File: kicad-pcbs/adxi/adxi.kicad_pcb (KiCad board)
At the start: 4 copper layers, 129.7 x 130 mm, 463 parts, among them J1 BNC, J2 PA-SUPPLY, J3 USBC, J4 PA-DRAIN, J5 USB2 Type-A, J6 RFC-GND, J7 12-24V SUPPLY, Q1 MMBF170, Q2 HY1904C2, Q3 2N7002, Q33 2N7002, Q34 HY1904C2, Q35 2N7002, Q36 HY1904C2, Q37 2N7002, Q38 HY1904C2, Q39 2N7002, Q4 HY1904C2, Q40 HY1904C2, Q41 2N7002, Q42 HY1904C2, Q43 2N7002, Q44 HY1904C2, Q45 2N7002, Q46 HY1904C2, Q47 2N7002, Q48 HY1904C2, Q49 2N7002, Q50 HY1904C2, Q51 2N7002, Q52 HY1904C2, Q53 2N7002, Q54 HY1904C2, Q55 2N7002, Q56 HY1904C2, Q57 2N7002, Q58 HY1904C2, Q59 2N7002, Q60 HY1904C2, U1 SI5351A-B-GTR, U10 CM108B, U11 93C46, U2 CD2003, U4 74ACT244, U5 74HC595, U7 TUSB321, U8 MT3608B, U9 SL2.1s, Y1 12MHz, Y2 25MHz

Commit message: Improvements to receiver
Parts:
- removed U11: 93C46, Package_SO:TSSOP-8_4.4x3mm_P0.65mm
- added C10: 100nF, Capacitor_SMD:C_0805_2012Metric, F.Cu at (87.0, 84.5)
- added C11: 220pF, Capacitor_SMD:C_0603_1608Metric, F.Cu at (44.8, 79.6)
- added C12: 100uF, Capacitor_SMD:C_1206_3216Metric, F.Cu at (100.6, 71.8)
- added C13: 100nF, Capacitor_SMD:C_0805_2012Metric, F.Cu at (79.1, 77.1)
- added C17: 10nF, Capacitor_SMD:C_0603_1608Metric, F.Cu at (57.1, 65.9)
- added C19: 10nF, Capacitor_SMD:C_0603_1608Metric, F.Cu at (59.6, 65.9)
- added C26: 1uF, Capacitor_SMD:C_0603_1608Metric, F.Cu at (102.3, 79.5)
- added C27: 100nF, Capacitor_SMD:C_0603_1608Metric, F.Cu at (103.4, 75.6)
- added C28: 10nF, Capacitor_SMD:C_0603_1608Metric, F.Cu at (62.1, 65.9)
- added C32: 100nF, Capacitor_SMD:C_0805_2012Metric, F.Cu at (129.5, 130.3)
- added C37: 10nF, Capacitor_SMD:C_0603_1608Metric, F.Cu at (64.7, 65.9)
- added C38: 100nF, Capacitor_SMD:C_0805_2012Metric, F.Cu at (109.2, 79.7)
- added C39: 220pF, Capacitor_SMD:C_0603_1608Metric, F.Cu at (47.3, 79.6)
- added C40: 220pF, Capacitor_SMD:C_0603_1608Metric, F.Cu at (49.8, 79.6)
- added C55: 1uF, Capacitor_SMD:C_0603_1608Metric, F.Cu at (104.8, 79.5)
- added C7: 100nF, Capacitor_SMD:C_0805_2012Metric, F.Cu at (108.3, 71.1)
- added C9: 100nF, Capacitor_SMD:C_0805_2012Metric, F.Cu at (108.3, 74.1)
- added R24: 10K, Resistor_SMD:R_0402_1005Metric, F.Cu at (112.5, 71.5)
- added R25: 10K, Resistor_SMD:R_0402_1005Metric, F.Cu at (112.5, 73.5)
- added U3: L7812, Package_TO_SOT_SMD:TO-263-2, F.Cu at (168.8, 82.2)
- U2: footprint Package_SO:SOP-16_4.55x10.3mm_P1.27mm -> Package_SO:SOP-16_3.9x9.9mm_P1.27mm
- moved U2 26.6 mm to (78.1, 84.4)
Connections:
- U10 pad 2: Net-(U10-DR) -> unconnected-(U10-DR-Pad2)
- U10 pad 3: Net-(U10-DW) -> unconnected-(U10-DW-Pad3)
- U10 pad 4: Net-(U10-SK) -> unconnected-(U10-SK-Pad4)
- U10 pad 5: Net-(U10-CS) -> unconnected-(U10-CS-Pad5)
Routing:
- net Net-(D5-K): track 15.0 -> 2.09 mm
- net unconnected-(U10-DR-Pad2): track 0.00 -> 2.51 mm
- net Net-(U10-DR): track 2.51 -> 0.00 mm
- net unconnected-(U10-DW-Pad3): track 0.00 -> 2.38 mm
- net Net-(U10-DW): track 2.38 -> 0.00 mm
- net unconnected-(U10-SK-Pad4): track 0.00 -> 2.33 mm
- net Net-(U10-SK): track 2.33 -> 0.00 mm
- net unconnected-(U10-CS-Pad5): track 0.00 -> 1.80 mm
- net Net-(U10-CS): track 1.80 -> 0.00 mm
- net Net-(D5-A): track 3.96 -> 2.61 mm

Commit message: More work, getting close now!
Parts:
- removed C22: 10uF, Capacitor_SMD:C_1206_3216Metric
- removed C60: 68nF, Capacitor_SMD:C_1206_3216Metric
- removed C61: 82pF, Capacitor_SMD:C_1206_3216Metric
- removed C62: 150pF, Capacitor_SMD:C_1206_3216Metric
- removed C8: 5.6nF, Capacitor_SMD:C_1206_3216Metric
- removed D27, D28, D29, D30, D31, D32, D33, D34, D35, D36, D37, D38, D39, D40: BZT52C12, Diode_SMD:D_SOD-123
- removed FB3: 100mΩ/3A, Capacitor_SMD:C_1206_3216Metric
- removed J1: BNC, Connector_Coaxial:BNC_TEConnectivity_1478204_Vertical
- removed L227, L228, L229, L230, L231, L232, L233, L234, L235, L236, L237, L238, L239, L240, L241, L242, L243, L244, L245, L246, L247, L248, L249, L250, L251, L252, L253, L254, L255, L256, L257, L258, L259, L260, L261, L262, L263, L264, L265, L266, L267, L268, L269, L270, L271, L272, L273, L274, L275, L276, L277, L278, L279, L280, L281, L282, L283, L284, L285, L286, L287, L288, L289, L290, L291, L292, L293, L294, L295, L296, L297, L298, L299, L300, L301, L302, L303, L304, L305, L306, L307, L308, L309, L310, L311, L312, L313, L314, L315, L316, L317, L318, L319, L320, L321, L322, L323, L324, L325, L326: 100nH, Inductor_SMD:L_1008_2520Metric
- removed L3: 100uH, Inductor_SMD:L_TaiTech_TMPC1265_13.5x12.5mm
- removed L327, L328, L329, L330, L331, L336, L337, L338, L339, L340, L345, L346, L347, L348, L349, L354, L355, L356, L357, L358: 10uH, Inductor_SMD:L_1008_2520Metric
- removed L332, L333, L334, L335, L341, L342, L343, L344, L350, L351, L352, L353, L359, L360, L361, L362: 100uH, Inductor_SMD:L_0805_2012Metric
- removed L363, L364, L365, L366, L367: 33nH, Inductor_SMD:L_1210_3225Metric
- removed L368, L369, L370, L371, L372, L373, L374, L375, L376, L377: 18nH, Inductor_SMD:L_1210_3225Metric
- removed L378, L379, L380, L381: 100uH, Inductor_SMD:L_Cenker_CKCS8040
- removed L382, L383, L384, L385, L386, L387, L388, L389, L390, L391, L392, L393, L394, L395, L396, L397, L398, L399, L400, L401, L402, L403, L404, L405, L406, L407, L408, L409, L410, L411, L412, L413, L414, L415, L416, L417, L418, L419, L420, L421, L422, L423, L424, L425, L426, L427, L428, L429, L430, L431, L432, L433, L434, L435, L436, L437, L438, L439, L440, L441, L442, L443, L444, L445, L446, L447: 470nH, Inductor_SMD:L_1008_2520Metric
- removed Q33, Q35, Q37, Q39, Q41, Q43, Q45, Q47, Q49, Q51, Q53, Q55, Q57, Q59: 2N7002, Package_TO_SOT_SMD:SOT-23
- removed Q34, Q36, Q38, Q40, Q42, Q44, Q46, Q48, Q50, Q52, Q54, Q56, Q58, Q60: HY1904C2, kicad-parts:HY1904C2
- removed R101, R102: 1K, Resistor_SMD:R_0603_1608Metric
- removed R103, R106, R107, R110, R111, R114, R115, R118, R119, R122, R123, R126, R127, R130, R131, R134, R135, R138, R139, R142, R143, R146, R147, R150, R151, R154, R155, R158: 1K 0.25W, Resistor_SMD:R_1206_3216Metric
- removed R104, R105, R108, R109, R112, R113, R116, R117, R120, R121, R124, R125, R128, R129, R132, R133, R136, R137, R140, R141, R144, R145, R148, R149, R152, R153, R156, R157: 6.8K 0.25W, Resistor_SMD:R_1206_3216Metric
- added C14: 470uF, Capacitor_SMD:C_Elec_10x10.2, F.Cu at (53.7, 114.4)
- added R26: 10, Resistor_SMD:R_1206_3216Metric, F.Cu at (44.1, 112.6)
- added R27: 22K, Resistor_SMD:R_0805_2012Metric, F.Cu at (74.0, 138.8)
- added R28: 22K, Resistor_SMD:R_0805_2012Metric, F.Cu at (75.7, 142.4)
- added R29: 22K, Resistor_SMD:R_0805_2012Metric, F.Cu at (73.5, 142.4)
- added R30: 100, Resistor_SMD:R_0805_2012Metric, F.Cu at (73.5, 145.9)
- added U6: LMV358CDRG, adxi-footprints:SOIC-8_L4.9-W3.9-P1.27-LS6.0-TL, F.Cu at (68.5, 140.8)
- C12: value 100uF -> 470uF; footprint Capacitor_SMD:C_1206_3216Metric -> Capacitor_SMD:C_Elec_10x10.2
- C2: value 6.8pF -> 100nF; footprint Capacitor_SMD:C_1206_3216Metric -> Capacitor_SMD:C_0603_1608Metric
- C21: value 100nF -> 10uF; footprint Capacitor_SMD:C_0805_2012Metric -> Capacitor_SMD:C_1206_3216Metric
- C3: value 12pF -> 10uF; footprint Capacitor_SMD:C_1206_3216Metric -> Capacitor_SMD:C_0603_1608Metric
- C4: value 15pF -> 100nF; footprint Capacitor_SMD:C_1206_3216Metric -> Capacitor_SMD:C_0603_1608Metric
- C6: value 20pF -> 100nF; footprint Capacitor_SMD:C_1206_3216Metric -> Capacitor_SMD:C_0603_1608Metric
- J7: footprint Connector_BarrelJack:BarrelJack_GCT_DCJ200-10-A_Horizontal -> adxi-footprints:DC-IN-TH_DC550250-0366-2H; moved to B.Cu
- L4: footprint Inductor_SMD:L_TaiTech_TMPC1265_13.5x12.5mm -> adxi-footprints:IND-SMD_L13.4-W12.6
- moved D11 228.6 mm to (29.1, 99.8), turned to 90 degrees
- moved C3 219.1 mm to (62.8, 140.3), turned to 180 degrees
- moved C2 215.3 mm to (62.8, 141.9), turned to 180 degrees
- moved C4 214.6 mm to (75.9, 138.7), turned to 90 degrees
- moved C6 211.8 mm to (75.7, 145.8), turned to 90 degrees
- moved D10 200.8 mm to (149.9, 102.6), turned to 90 degrees
- moved C58 162.7 mm to (39.5, 137.4), turned to 180 degrees
- moved C59 162.2 mm to (39.5, 139.1), turned to 180 degrees
- moved C25 142.7 mm to (136.7, 141.4), turned to 90 degrees
- moved L4 140.0 mm to (122.9, 144.7), turned to 180 degrees
- moved C23 139.5 mm to (140.5, 137.6), turned to -90 degrees
- moved C18 138.5 mm to (133.7, 131.8), turned to 90 degrees
- moved C44 138.2 mm to (66.9, 150.2), turned to -135 degrees
- moved C48 138.0 mm to (59.9, 132.5), turned to 180 degrees
- moved C45 137.4 mm to (67.0, 146.6), turned to -135 degrees
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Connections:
- net PDSW renamed SLEEP-WHEN-LOW
- net VOLDN renamed VOLUME-DOWN-BUTTON-WHEN-LOW
- C12 pad 1: 5V -> Net-(D5-K)
- C16 pad 2: 5V -> Net-(D5-K)
- C2 pad 1: /pa-lpf-ant/PA Switched Resonator1/PA-RESONATOR-C-6.8PF/LOAD-ANODE -> 5V
- C2 pad 2: /pa-lpf-ant/PA Switched Resonator1/PA-DRAIN -> GND
- C3 pad 1: /pa-lpf-ant/PA Switched Resonator1/PA-RESONATOR-C-12PF/LOAD-ANODE -> 5V
- C3 pad 2: /pa-lpf-ant/PA Switched Resonator1/PA-DRAIN -> GND
- C4 pad 1: /pa-lpf-ant/PA Switched Resonator1/PA-RESONATOR-C-15PF/LOAD-ANODE -> Net-(U10-LOL)
- C4 pad 2: /pa-lpf-ant/PA Switched Resonator1/PA-DRAIN -> Net-(C4-Pad2)
- C6 pad 1: /pa-lpf-ant/PA Switched Resonator1/PA-RESONATOR-C-20PF/LOAD-ANODE -> Net-(U10-LOR)
- C6 pad 2: /pa-lpf-ant/PA Switched Resonator1/PA-DRAIN -> Net-(C6-Pad2)
- D11 pad 2: PA-DRAIN -> RECEIVED-SIGNAL
- J4 pad 1: PA-DRAIN -> RECEIVED-SIGNAL
- J4 pad 2: PA-DRAIN -> RECEIVED-SIGNAL
- J4 pad 3: PA-DRAIN -> RECEIVED-SIGNAL
- J4 pad 4: PA-DRAIN -> RECEIVED-SIGNAL
- R1 pad 2: PA-DRAIN -> RECEIVED-SIGNAL
- R9 pad 2: PA-DRAIN -> RECEIVED-SIGNAL
- TP13 pad 1: PA-DRAIN -> RECEIVED-SIGNAL
- U10 pad 31: HOST-FSK-BIAS -> /1.75V-BIAS
- U7 pad 6: IFAULT-WHEN-LOW -> unconnected-(U7-~{VCONN_FAULT}-Pad6)
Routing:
- net GND: track 25.8 -> 0.00 mm, vias 17 -> 0
- net 3.3V: track 16.6 -> 0.00 mm, vias 2 -> 0
- net Net-(D9-K): track 12.6 -> 0.00 mm, vias 2 -> 0
- net TX-CLK: track 10.5 -> 0.00 mm
- net 1.8V: track 8.08 -> 0.00 mm
- net Net-(Q3-D): track 8.05 -> 0.00 mm
- net 24V: track 6.41 -> 0.00 mm
- net Net-(U9-XIN): track 6.37 -> 0.00 mm
- net Net-(U9-XOUT): track 6.30 -> 0.00 mm
- net SLEEP-WHEN-LOW: track 5.79 -> 0.00 mm, vias 2 -> 0
- net REVERSE-POWER: track 5.50 -> 0.00 mm
- net Net-(U10-USBDM): track 5.21 -> 0.00 mm
- net /Late Stage Interface/PA-SUPPLY: track 4.97 -> 0.00 mm
- net USB-C-USB2-D+: track 4.39 -> 0.00 mm
- net USB-CM108-D-: track 4.06 -> 0.00 mm
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- added copper zone on B.Cu, net GND
- added copper zone on F.Cu, net GND
- removed copper zone on F.Cu, net (none)
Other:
- outline, holes or cut-outs redrawn
- board text added: "("
- board text added: "1"
- board text added: "1.0"
- board text added: "12V"
- board text added: "2"
- board text added: "3"
- board text added: "3.3V"
- board text added: "5V"
- board text added: "FWP"
- board text added: "KEEP CLEAR OF METAL"
- board text added: "PA+"
- board text added: "PA-DRAIN"
- board text added: "PA-SUPPLY"
- board text added: "RESONANCE AREA"
- board text added: "RFC-"
- board text added: "RFC-GND"
- board text added: "RVP"
- board text added: "RX"
- board text added: "USBC"
- board text added: "USBC CLEAN"
- board text added: "USBC VIN"
- board text added: "VIN-CLAMP"
- board text removed: "BNC"
- board text removed: "FORWARD"
- board text removed: "MCU"
- board text removed: "MMCX"
- board text removed: "PA"
- board text removed: "PHYSICAL INTERFACE PROTOTYPE"
- board text removed: "RESONATOR CONFIGURATIONS"
- board text removed: "REVERSE"
- board text removed: "RF CHOKE CONFIGURATIONS"
- board text removed: "SMA"
- board text removed: "SWR"
- board text removed: "TEST POINTS"
- board text removed: "USB AUDIO"
- board text removed: "USB-C-PD"

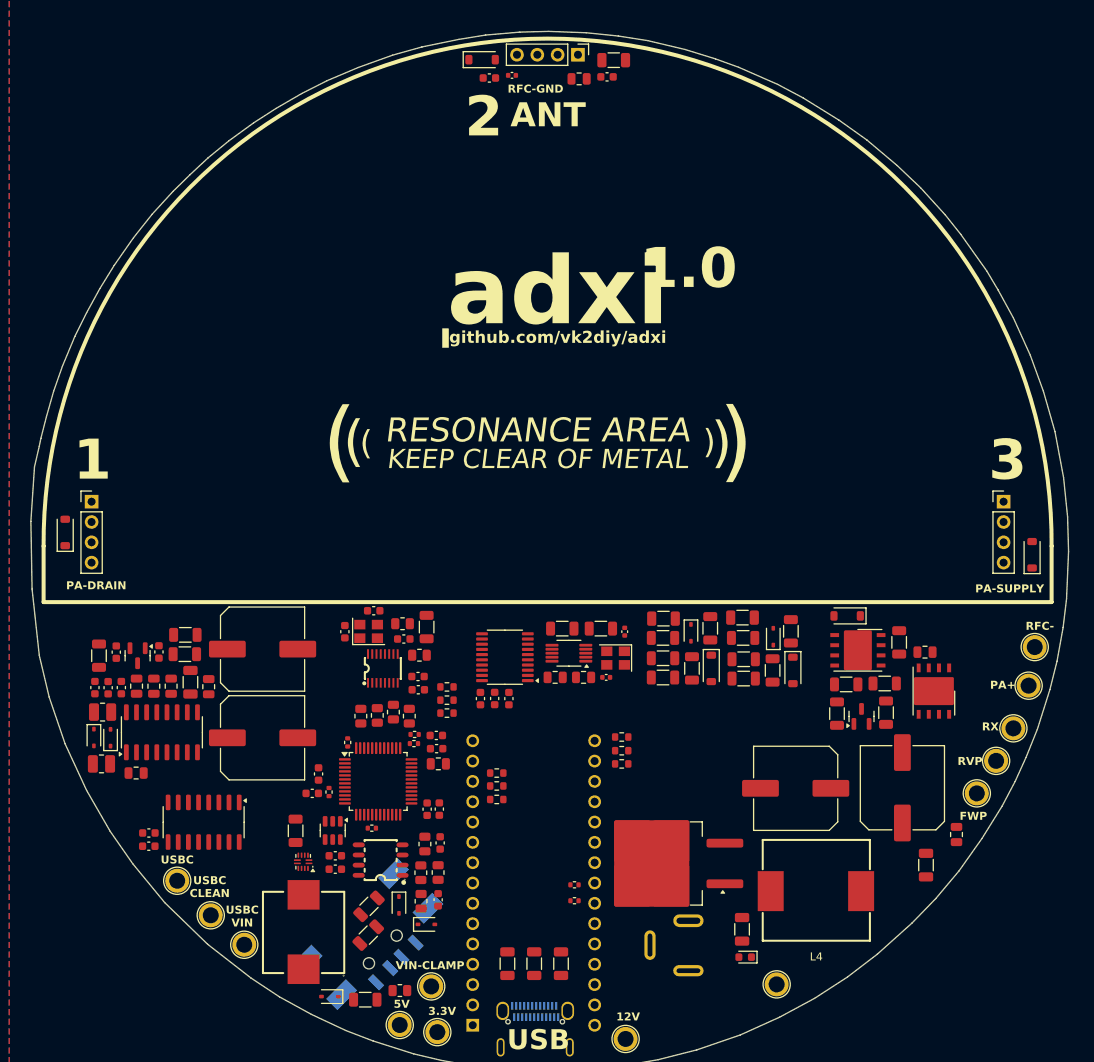
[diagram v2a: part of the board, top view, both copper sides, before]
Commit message: Simplify PSU, add 4xM3 mounting holes, silkscreen, better footprints
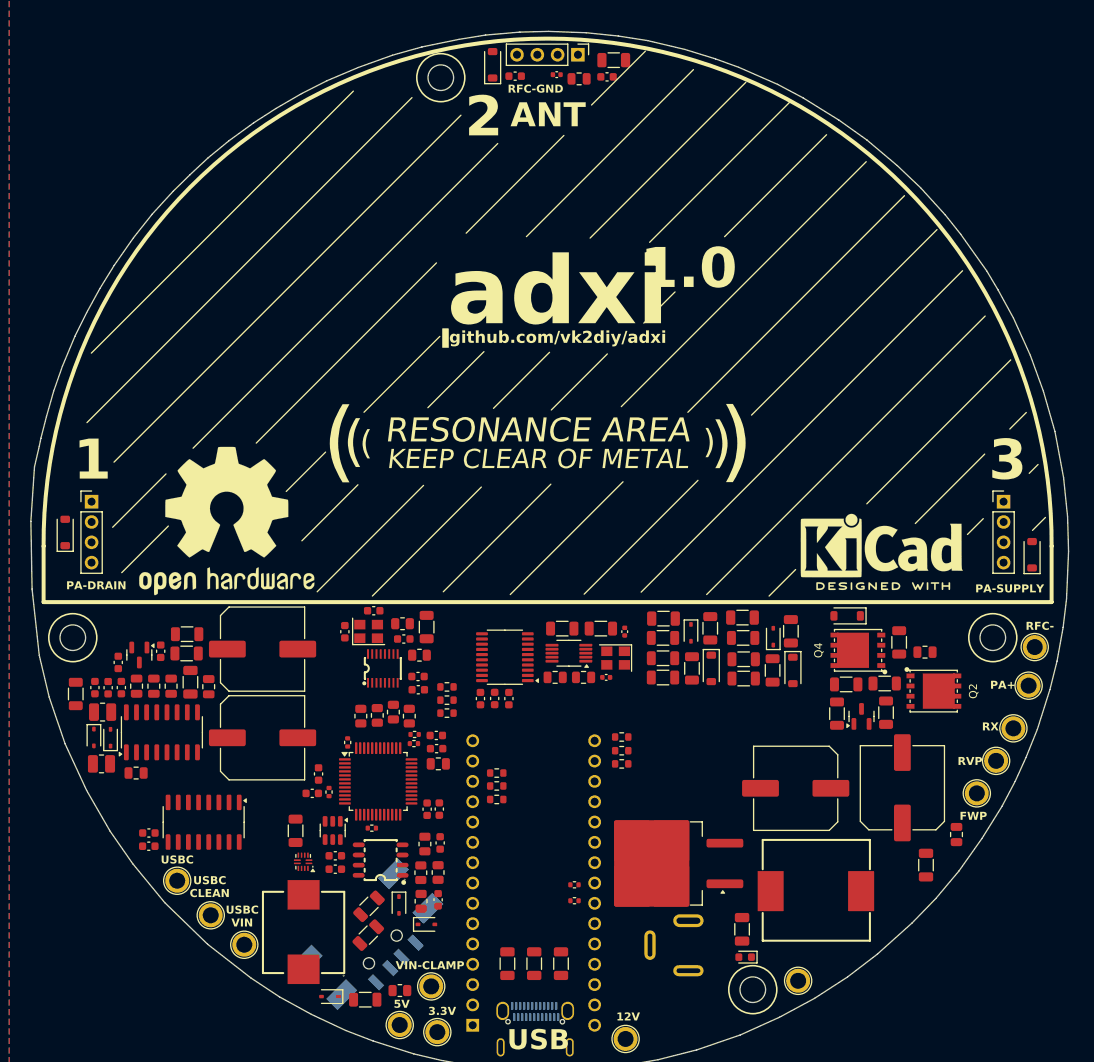
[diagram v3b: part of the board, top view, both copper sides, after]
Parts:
- added H1: M3 NPTH, MountingHole:MountingHole_3.2mm_M3_DIN965, F.Cu at (115.0, 157.0)
- added H2: M3 NPTH, MountingHole:MountingHole_3.2mm_M3_DIN965, F.Cu at (30.0, 113.0)
- added H3: M3 NPTH, MountingHole:MountingHole_3.2mm_M3_DIN965, F.Cu at (76.0, 43.0)
- added H4: M3 NPTH, MountingHole:MountingHole_3.2mm_M3_DIN965, F.Cu at (145.0, 113.0)
- added REF**: OSHW-Logo2_24.3x20mm_SilkScreen, Symbol:OSHW-Logo2_24.3x20mm_SilkScreen, F.Cu at (49.2, 98.4)
- added REF**: KiCad-Logo2_8mm_SilkScreen, Symbol:KiCad-Logo2_8mm_SilkScreen, F.Cu at (131.1, 101.5)
- Q2, Q4: footprint kicad-parts:HY1904C2 -> adxi-footprints:DFN-8_L5.9-W5.2-P1.27-LS6.2-BL
- moved R14 5.60 mm to (30.4, 120.0), turned to -90 degrees
- moved C34 5.59 mm to (90.5, 42.6)
- moved C33 3.23 mm to (85.3, 42.8)
- moved TP2 2.72 mm to (120.7, 155.9)
- moved D8 1.47 mm to (82.5, 41.4), turned to 90 degrees
- moved C19 1.31 mm to (35.7, 116.1)
- moved R26 0.24 mm to (44.3, 112.6)
- moved C17 0.24 mm to (41.0, 114.7)
- moved Q1 0.24 mm to (38.3, 115.2)
- moved R13 0.24 mm to (44.2, 115.0)
- turned Q4 to 90 degrees
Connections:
- Q2 pad 5: PA-DRAIN -> RECEIVED-SIGNAL
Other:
- board text removed: "5 TIER CHINESE TIFFIN LUNCH BOX"
- board text removed: "https://www.aliexpress.com/item/1005006756495960.html https://www.aliexpress.com/item/1005006075889043.html"

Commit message: Layout complete
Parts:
- removed D24, D25: 1N4148WS, Diode_SMD:D_SOD-323
- removed D7: 24V 1ns, Diode_SMD:D_0603_1608Metric
- removed FB1: 100mΩ/3A, Capacitor_SMD:C_1206_3216Metric
- removed J7: 12-24V SUPPLY, adxi-footprints:DC-IN-TH_DC550250-0366-2H
- removed TP2: VIN-COM, TestPoint:TestPoint_Plated_Hole_D2.0mm
- added C8: 470uF, Capacitor_SMD:C_Elec_10x10.2, F.Cu at (134.8, 130.0)
- TP5: value VIN-CLAMPED -> VIN
- moved Q2 101.9 mm to (36.4, 108.6), turned to 135 degrees
- moved R15 91.0 mm to (42.4, 110.2), turned to 0 degrees
- moved C32 90.1 mm to (46.5, 110.3)
- moved TP5 59.2 mm to (133.1, 146.2)
- moved C18 26.1 mm to (108.3, 125.7), turned to 180 degrees
- moved R16 13.4 mm to (138.1, 117.9), turned to 180 degrees
- moved Q3 12.7 mm to (138.4, 114.9), turned to 180 degrees
- moved R17 12.3 mm to (138.0, 111.8), turned to 0 degrees
- moved C23 9.92 mm to (131.2, 141.2), turned to 180 degrees
- moved TP1 8.04 mm to (106.9, 161.1)
- moved R19 8.03 mm to (134.4, 116.8), turned to 90 degrees
- moved R18 7.33 mm to (134.3, 112.0), turned to 90 degrees
- moved U3 6.56 mm to (103.8, 147.8)
- moved C25 5.59 mm to (131.8, 138.7), turned to 180 degrees
- moved D9 2.25 mm to (129.0, 110.4), turned to 0 degrees
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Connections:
- C18 pad 1: /VIN-COMMON -> /VIN-USBC
- C20 pad 1: /VIN-COMMON -> /VIN-USBC
- C23 pad 2: /VIN-COMMON -> /VIN-USBC
- C25 pad 2: /VIN-COMMON -> /VIN-USBC
- L4 pad 1: /VIN-COMMON -> /VIN-USBC
- TP5 pad 1: /VIN-CLAMPED -> /VIN
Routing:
- net 3.3V: track 0.00 -> 241.6 mm, vias 0 -> 12
- net GND: track 0.00 -> 179.7 mm, vias 0 -> 107
- net RECEIVED-SIGNAL: track 0.00 -> 158.7 mm, vias 0 -> 1
- net 5V: track 0.00 -> 156.7 mm, vias 0 -> 6
- net /VIN-USBC: track 0.00 -> 152.1 mm, vias 0 -> 6
- net 12V: track 0.00 -> 145.3 mm, vias 0 -> 7
- net /Late Stage Interface/RFC-GND: track 0.00 -> 135.7 mm
- net FORWARD-POWER: track 0.00 -> 93.9 mm, vias 0 -> 3
- net REVERSE-POWER: track 0.00 -> 82.2 mm, vias 0 -> 2
- net SPI-SCK-3.3V: track 0.00 -> 80.5 mm, vias 0 -> 4
- net PA-DRIVE-PWM: track 0.00 -> 80.3 mm, vias 0 -> 4
- net Net-(D5-K): track 0.00 -> 67.3 mm
- net RECEIVE-ENABLE: track 0.00 -> 61.8 mm, vias 0 -> 4
- net Net-(U4-1Y0): track 0.00 -> 60.5 mm
- net SPI-SS-OUTPUTS-3.3V: track 0.00 -> 56.8 mm, vias 0 -> 6
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- added copper zone on In1.Cu, net GND
- added copper zone on In2.Cu, net GND
- removed copper zone on F.Cu, net GND
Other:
- board text added: "RESONANCE ZONE"
- board text added: "VIN"
- board text removed: "RESONANCE AREA"
- board text removed: "VIN-CLAMP"

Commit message: Fixed vias
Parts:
- added TP14: GND, TestPoint:TestPoint_THTPad_2.0x2.0mm_Drill1.0mm, F.Cu at (36.3, 134.3)
- added TP15: GND, TestPoint:TestPoint_THTPad_2.0x2.0mm_Drill1.0mm, F.Cu at (110.5, 160.8)
- added TP2: GND, TestPoint:TestPoint_THTPad_2.0x2.0mm_Drill1.0mm, F.Cu at (137.9, 140.4)
- TP1, TP10, TP11, TP12, TP13, TP3, TP4, TP5, TP6, TP7, TP8, TP9: footprint TestPoint:TestPoint_Plated_Hole_D2.0mm -> TestPoint:TestPoint_THTPad_2.0x2.0mm_Drill1.0mm
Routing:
- net PA-DRIVE-PWM: track 80.3 -> 105.2 mm
- net GND: track 179.7 -> 181.9 mm, vias 107 -> 108
- net RX-CLK: track 53.7 -> 52.0 mm
- net 3.3V: track 241.6 -> 243.2 mm, vias 12 -> 13
- net 5V: track 156.7 -> 158.1 mm
- net SPI-SS-OUTPUTS-3.3V: track 56.8 -> 55.6 mm
- net VOLUME-DOWN-BUTTON-WHEN-LOW: track 19.8 -> 20.5 mm
- net MUTE-PLAYBACK-WHEN-LOW: track 30.8 -> 31.5 mm
- net /1.75V-BIAS: track 12.3 -> 12.9 mm
- net USB-C-VBUS: track 38.7 -> 38.1 mm
- net Net-(FB6-Pad1): track 12.5 -> 13.1 mm
- net RECEIVED-AUDIO: track 40.2 -> 40.8 mm
- net FORWARD-POWER: track 93.9 -> 94.6 mm
- net Net-(U10-USBDP): track 4.00 -> 4.30 mm, vias 2 -> 0
- net SLEEP-WHEN-LOW: track 33.2 -> 33.0 mm, vias 3 -> 4
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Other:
- board text added: "ARDUINO NANO v3 (ATMEGA328P MODULE)"
- board text added: "DIGITAL MODES COMPUTER ASSISTED TRANSCEIVER"
- board text added: "FSKIN"
- board text added: "GND"
- board text added: "IMODE1"
- board text added: "IMODE2"
- board text added: "LEDO"
- board text added: "LEDR"
- board text added: "M3 STANDOFF >=20MM"
- board text added: "M3 STANDOFF >=20MM (NYLON/POLYMER PREFERRED)"
- board text added: "MOSI"
- board text added: "NC.A2"
- board text added: "NC.A3"
- board text added: "NC.A6"
- board text added: "NC.A7"
- board text added: "NC.AREF"
- board text added: "NC.D0"
- board text added: "NC.D1"
- board text added: "NC.D10"
- board text added: "NC.D6"
- board text added: "NC.RST28"
- board text added: "NC.RST3"
- board text added: "PAPWM"
- board text added: "RX~{EN}"
- board text added: "SCK"
- board text added: "SCL"
- board text added: "SDA"
- board text added: "SS-OUT"
- board text added: "USB2 TYPE-A TO USB2-MINI CABLE"
